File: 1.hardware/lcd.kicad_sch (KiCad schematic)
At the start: 34 parts, among them J6 FPC_LCD_40

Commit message: 중간 저장
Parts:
- added C100: 0.1uF/50V, Capacitor_SMD:C_0603_1608Metric, symbol Device:C_Small_US
- added C99: 1uF/10V, Capacitor_SMD:C_0603_1608Metric, symbol Device:C_Small_US
- added R170: 10k/0.063w, Resistor_SMD:R_0402_1005Metric, symbol Device:R_Small_US
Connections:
- net LCD_VCI is gone; now on net 3V3: J6.5 (Pin_5)
- net TP_VCI is gone; now on net 3V3: J6.39 (Pin_39)
- net GND: now also C100.2, C99.2
- net LCD_DISP: now also R170.2
- net 3V3_PWR renamed 3V3
- net 3V3: now also C100.1, C99.1, R170.1

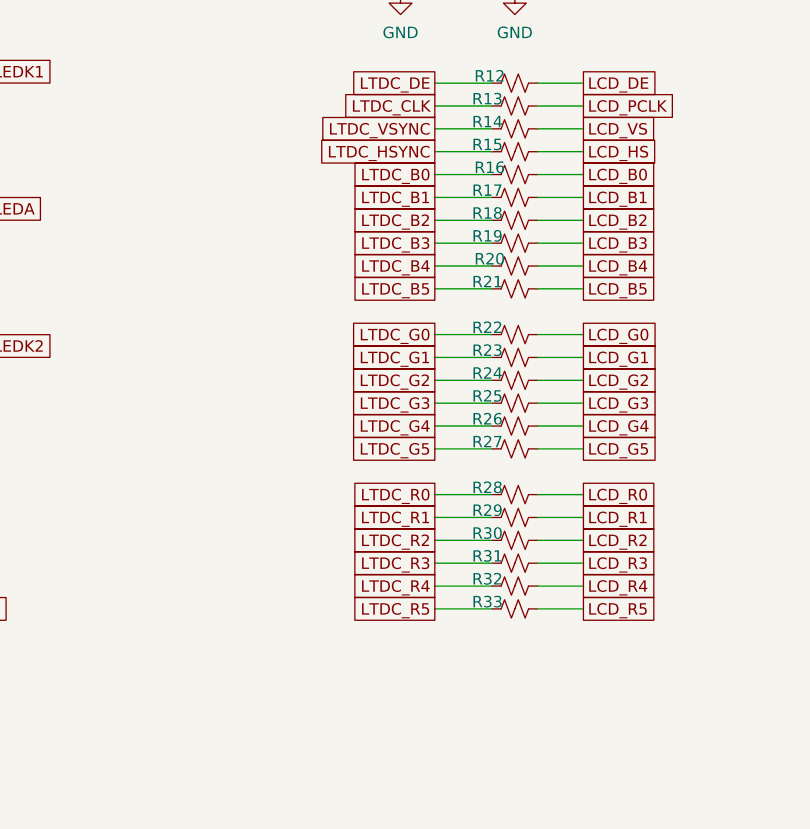
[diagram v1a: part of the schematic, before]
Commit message: 핀 배치 반영
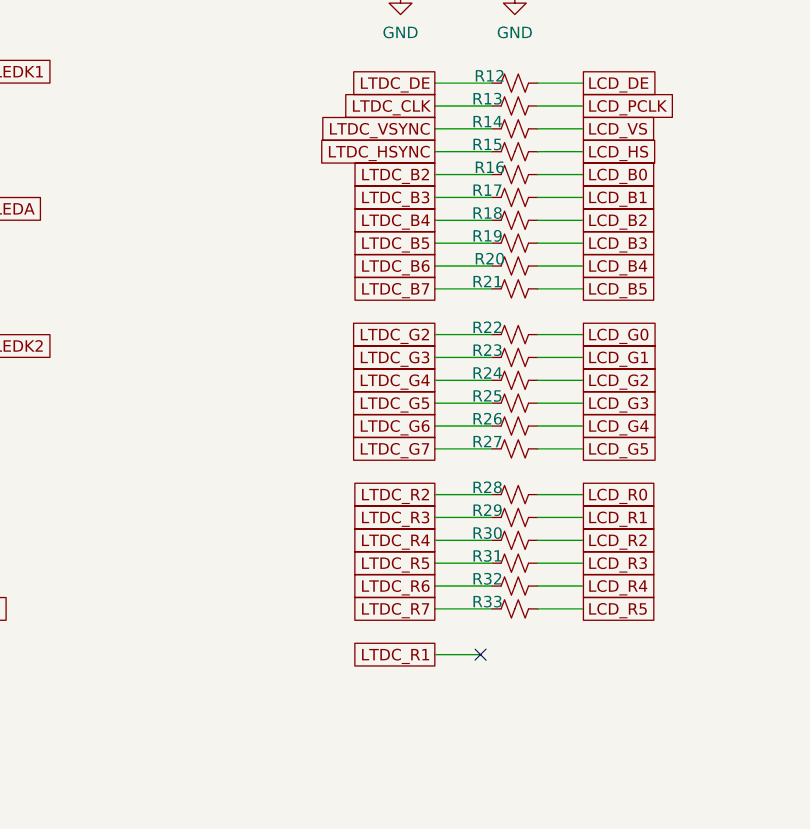
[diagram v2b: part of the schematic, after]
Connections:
- net LTDC_B0 is gone; now on net LTDC_B2: R16.1
- net LTDC_B1 is gone; now on net LTDC_B3: R17.1
- net LTDC_G0 is gone; now on net LTDC_G2: R22.1
- net LTDC_G1 is gone; now on net LTDC_G3: R23.1
- net LTDC_R0 is gone; now on net LTDC_R2: R28.1
- net LTDC_B2: no longer R18.1
- net LTDC_B3: no longer R19.1
- net LTDC_B4: now also R18.1; no longer R20.1
- net LTDC_B5: now also R19.1; no longer R21.1
- net LTDC_G2: no longer R24.1
- net LTDC_G3: no longer R25.1
- net LTDC_G4: now also R24.1; no longer R26.1
- net LTDC_G5: now also R25.1; no longer R27.1
- net LTDC_R1: no longer R29.1
- net LTDC_R2: no longer R30.1
- net LTDC_R3: now also R29.1; no longer R31.1
- net LTDC_R4: now also R30.1; no longer R32.1
- net LTDC_R5: now also R31.1; no longer R33.1
- new net LTDC_B6: R20.1
- new net LTDC_B7: R21.1
- new net LTDC_G6: R26.1
- new net LTDC_G7: R27.1
- new net LTDC_R6: R32.1
- new net LTDC_R7: R33.1
- no-connect marks 5 -> 6

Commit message: 중간 저장
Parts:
- R106: renamed from R10; value 10.2R -> 10.2R/0.125w; footprint (none) -> Resistor_SMD:R_0805_2012Metric
- R107: renamed from R11; value 10.2R -> 10.2R/0.125w; footprint (none) -> Resistor_SMD:R_0805_2012Metric
- renumbered C38 to C74, C39 to C75, C40 to C76, C100 to C77, C99 to C78, D7 to D12, D8 to D13, J6 to J12, L8 to L10, L7 to L9, PS1 to PS4, PS2 to PS5, R170 to R108, R12 to R109, R13 to R110, R14 to R111, R15 to R112, R16 to R113, R17 to R114, R18 to R115, R19 to R116, R20 to R117, R21 to R118, R22 to R119, R23 to R120, R24 to R121, R25 to R122, R26 to R123, R27 to R124, R28 to R125, R29 to R126, R30 to R127, R31 to R128, R32 to R129, R33 to R130

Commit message: 중간 저장
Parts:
- J12: value FPC_LCD_40 -> FPC_LCD_40_CONN
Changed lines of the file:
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@@
 			)
 		)
-		(property "Value" "FPC_LCD_40"
+		(property "Value" "FPC_LCD_40_CONN"
 			(at 312.42 115.5699 0)
 			(effects

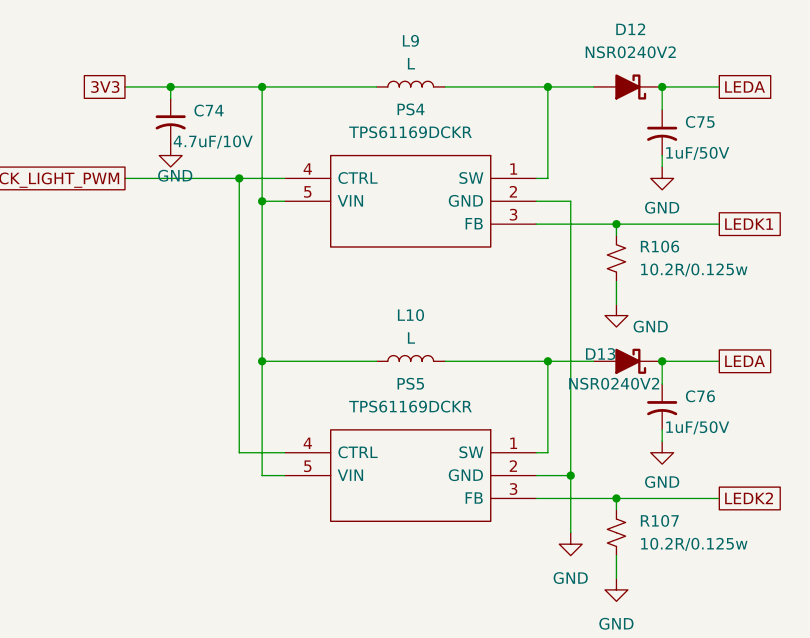
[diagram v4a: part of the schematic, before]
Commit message: 풋프린트 연결 완료
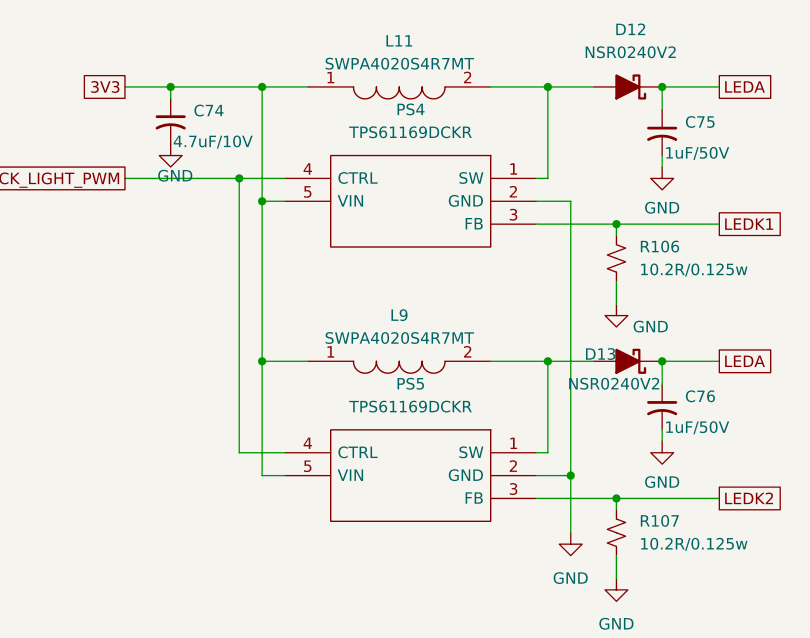
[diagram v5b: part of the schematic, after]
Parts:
- removed L10, L9: L, symbol Device:L
- added L11, L9: SWPA4020S4R7MT, SamacSys_Parts_Project:INDPM4040X200N, symbol SamacSys_Parts:SWPA4020S4R7MT
- J12: footprint (none) -> Connector_FFC-FPC:Amphenol_F32Q-1A7x1-11040_1x40-1MP_P0.5mm_Horizontal
- PS4, PS5: footprint SamacSys_Parts:SOT65P210X110-5N -> SamacSys_Parts_Project:SOT65P210X110-5N
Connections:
- net 3V3: now also L11.1, L9.1
- net at D12.2 (A), PS4.1 (SW): now also L11.2
- net at D13.2 (A), PS5.1 (SW): now also L9.2

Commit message: 중간 저장
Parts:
- renumbered C74 to C76, C75 to C77, C76 to C78, C77 to C79, C78 to C80, D12 to D11, D13 to D12, L9 to L10, L11 to L9, R112 to R100, R113 to R101, R114 to R102, R115 to R103, R116 to R104, R117 to R105, R118 to R106, R119 to R107, R120 to R108, R121 to R109, R122 to R110, R123 to R111, R124 to R112, R125 to R113, R126 to R114, R127 to R115, R128 to R116, R129 to R117, R130 to R118, R106 to R94, R107 to R95, R108 to R96, R109 to R97, R110 to R98, R111 to R99

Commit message: 중간 저장
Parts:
- added H5, H6, H7: MountingHole, MountingHole:MountingHole_2.5mm, symbol Mechanical:MountingHole
- C80: value 1uF/10V -> 1uF/50V
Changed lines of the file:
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@@
+	)
+	(symbol
+		(lib_id "Mechanical:MountingHole")
+		(at 135.89 45.72 0)
+		(unit 1)
+		(exclude_from_sim no)
+		(in_bom no)
+		(on_board yes)
+		(dnp no)
+		(fields_autoplaced yes)
+		(property "Reference" "H5"
+			(at 138.43 44.4499 0)
+			(effects
+				(font
+					(size 1.27 1.27)
+				)
+				(justify left)
+			)
+		)
+		(property "Value" "MountingHole"
+			(at 138.43 46.9899 0)
+			(effects
+				(font
+					(size 1.27 1.27)
+				)
+				(justify left)
+			)
+		)
+		(property "Footprint" "MountingHole:MountingHole_2.5mm"
+			(at 135.89 45.72 0)
+			(effects
+				(font
+					(size 1.27 1.27)
+				)
+				(hide yes)
+			)
+		)
+		(property "Datasheet" "~"
+			(at 135.89 45.72 0)
+			(effects
+				(font
+					(size 1.27 1.27)
+				)
+				(hide yes)
+			)
+		)
+		(property "Description" "Mounting Hole without connection"
+			(at 135.89 45.72 0)
+			(effects
+				(font
+					(size 1.27 1.27)
+				)
+				(hide yes)
+			)
+		)
+		(instances
+			(project ""
+				(path "/a25adab6-a8c3-4e0e-8ba9-baac00aaa394/9ad5d27a-5f31-4a09-b7fb-9d62ecc953c1"
+					(reference "H5")
+					(unit 1)
+				)
+			)
+		)
 	)
 	(symbol
@@
 				(path "/a25adab6-a8c3-4e0e-8ba9-baac00aaa394/9ad5d27a-5f31-4a09-b7fb-9d62ecc953c1"
 					(reference "R115")
+					(unit 1)
+				)
+			)
+		)
+	)
+	(symbol
+		(lib_id "Mechanical:MountingHole")
+		(at 171.45 45.72 0)
+		(unit 1)
+		(exclude_from_sim no)
+		(in_bom no)
+		(on_board yes)
+		(dnp no)
+		(fields_autoplaced yes)
+		(property "Reference" "H7"
+			(at 173.99 44.4499 0)
+			(effects
+				(font
+					(size 1.27 1.27)
+				)
+				(justify left)
+			)
+		)
+		(property "Value" "MountingHole"
+			(at 173.99 46.9899 0)
+			(effects
+				(font
+					(size 1.27 1.27)
+				)
+				(justify left)
+			)
+		)
+		(property "Footprint" "MountingHole:MountingHole_2.5mm"
+			(at 171.45 45.72 0)
+			(effects
+				(font
+					(size 1.27 1.27)
+				)
+				(hide yes)
+			)
+		)
+		(property "Datasheet" "~"
+			(at 171.45 45.72 0)
+			(effects
+				(font
+					(size 1.27 1.27)
+				)
+				(hide yes)
+			)
+		)
+		(property "Description" "Mounting Hole without connection"
+			(at 171.45 45.72 0)
+			(effects
+				(font
+					(size 1.27 1.27)
+				)
+				(hide yes)
+			)
+		)
+		(instances
+			(project "bldc_motor_controller"
+				(path "/a25adab6-a8c3-4e0e-8ba9-baac00aaa394/9ad5d27a-5f31-4a09-b7fb-9d62ecc953c1"
+					(reference "H7")
 					(unit 1)
 				)
@@
 			)
 		)
-		(property "Value" "1uF/10V"
+		(property "Value" "1uF/50V"
 			(at 256.794 72.136 0)
 			(effects
@@
 					(unit 1)
 				)
+			)
+		)
+	)
+	(symbol
+		(lib_id "Mechanical:MountingHole")
+		(at 153.67 45.72 0)
+		(unit 1)
+		(exclude_from_sim no)
+		(in_bom no)
+		(on_board yes)
+		(dnp no)
+		(fields_autoplaced yes)
+		(property "Reference" "H6"
+			(at 156.21 44.4499 0)
+			(effects
+				(font
+					(size 1.27 1.27)
+				)
+				(justify left)
+			)
+		)
+		(property "Value" "MountingHole"
+			(at 156.21 46.9899 0)
+			(effects
+				(font
+					(size 1.27 1.27)
+				)
+				(justify left)
+			)
+		)
+		(property "Footprint" "MountingHole:MountingHole_2.5mm"
+			(at 153.67 45.72 0)
+			(effects
+				(font
+					(size 1.27 1.27)
+				)
+				(hide yes)
+			)
+		)
+		(property "Datasheet" "~"
+			(at 153.67 45.72 0)
+			(effects
+				(font
+					(size 1.27 1.27)
+				)
+				(hide yes)
+			)
+		)
+		(property "Description" "Mounting Hole without connection"
+			(at 153.67 45.72 0)
+			(effects
+				(font
+					(size 1.27 1.27)
+				)
+				(hide yes)
+			)
+		)
+		(instances
+			(project "bldc_motor_controller"
+				(path "/a25adab6-a8c3-4e0e-8ba9-baac00aaa394/9ad5d27a-5f31-4a09-b7fb-9d62ecc953c1"
+					(reference "H6")
+					(unit 1)
+				)

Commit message: 중간 저장
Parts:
- renumbered C79 to C76, C80 to C77, C76 to C78, C77 to C79, C78 to C80, D11 to D10, D12 to D11, L9 to L8, L10 to L9, PS4 to PS3, PS5 to PS4, R106 to R100, R107 to R101, R108 to R102, R95 to R103, R109 to R104, R110 to R105, R111 to R106, R112 to R107, R113 to R108, R114 to R109, R115 to R110, R96 to R111, R116 to R112, R117 to R113, R118 to R114, R97 to R90, R94 to R91, R98 to R92, R99 to R93, R100 to R94, R101 to R95, R102 to R96, R103 to R97, R104 to R98, R105 to R99
